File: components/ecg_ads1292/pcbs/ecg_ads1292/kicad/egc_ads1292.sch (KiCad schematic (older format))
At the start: 32 parts, among them J1 n.p., J2 n.p., J3 n.p., J4 n.p., J5 Conn_02x06_Odd_Even

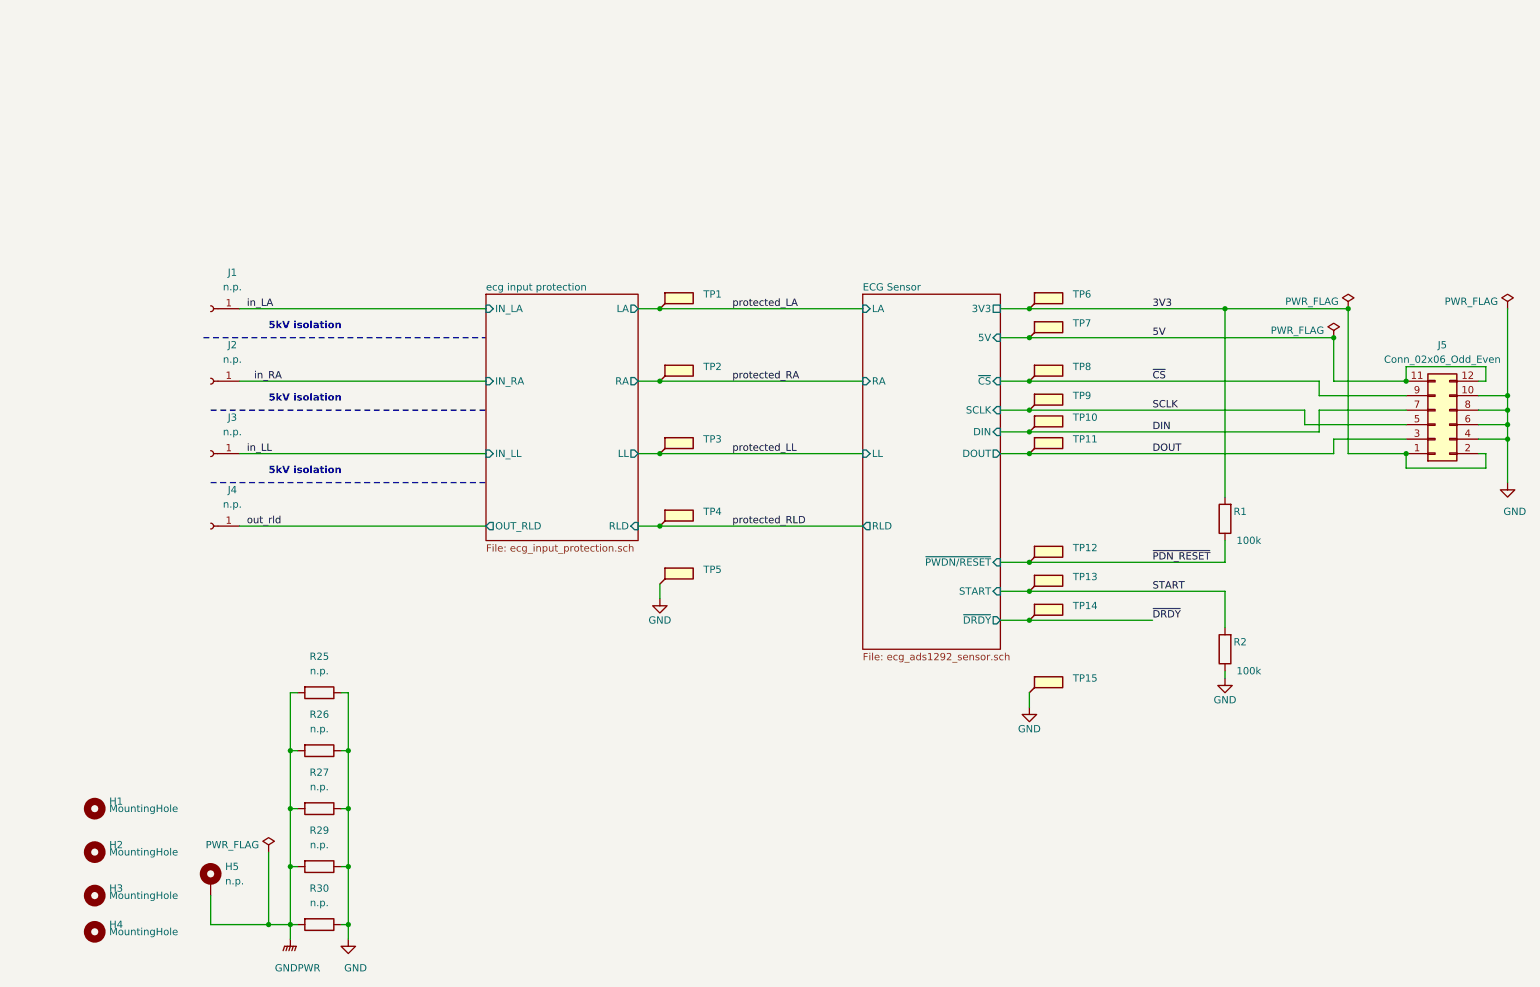
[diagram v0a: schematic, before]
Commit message: allow daisy chaining and improve ground planes
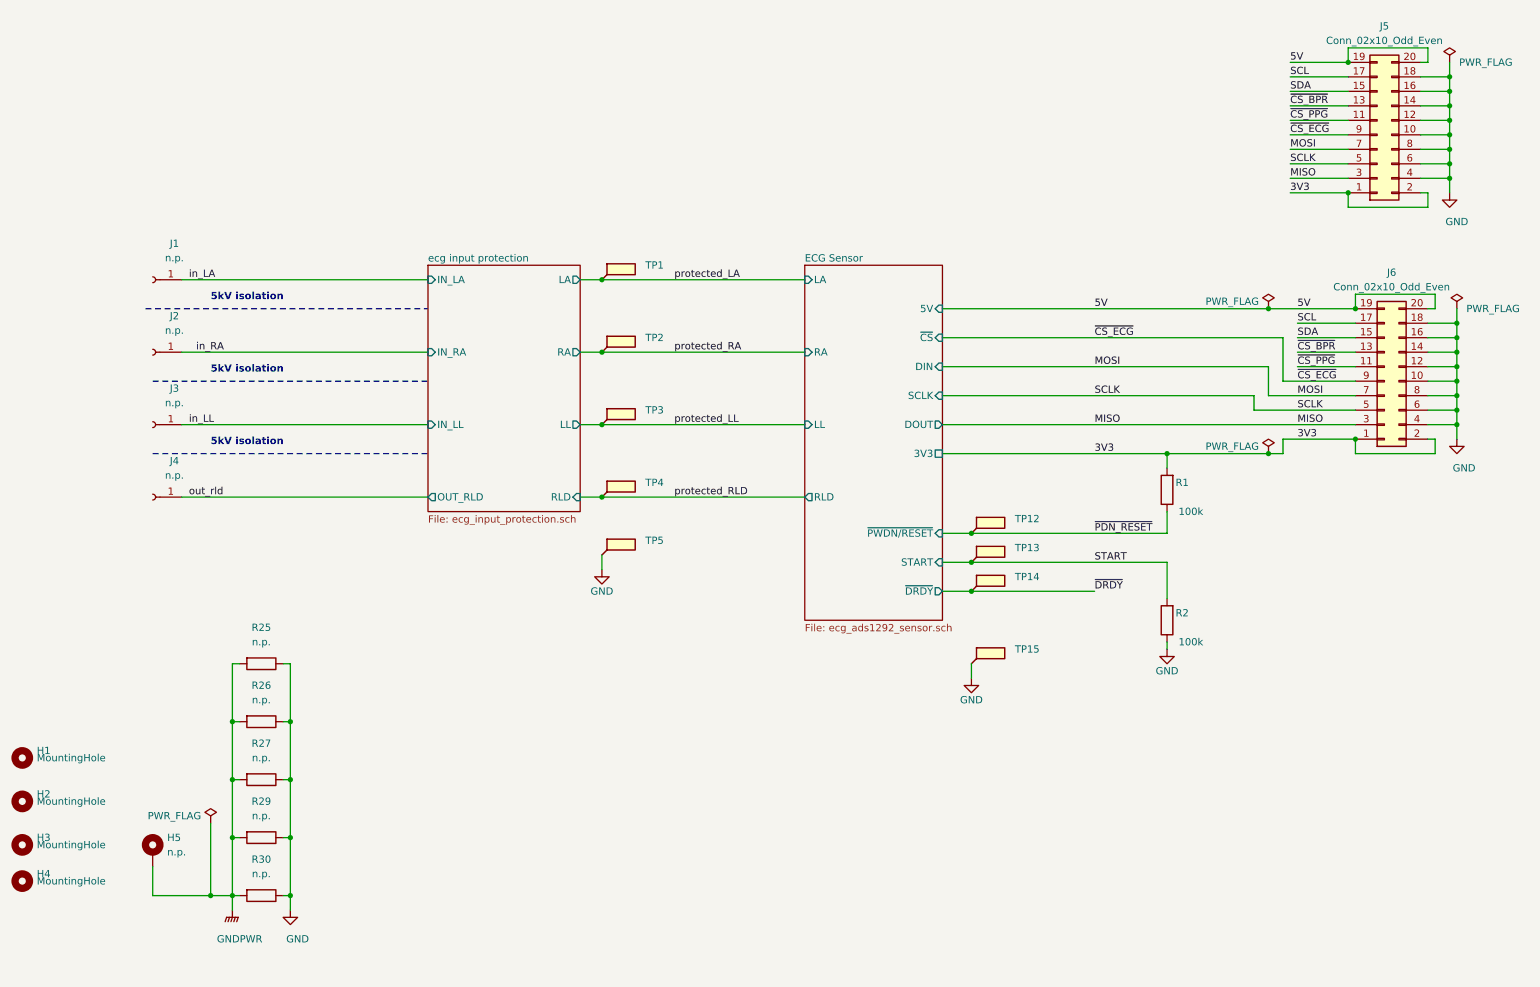
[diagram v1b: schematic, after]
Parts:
- removed J5: Conn_02x06_Odd_Even, Connector_PinHeader_2.54mm:PinHeader_2x06_P2.54mm_Vertical, symbol Connector_Generic:Conn_02x06_Odd_Even
- removed TP10, TP11, TP6, TP7, TP8, TP9: (no value), TestPoint:TestPoint_Loop_D2.50mm_Drill1.0mm, symbol Connector:TestPoint_Flag
- added J5, J6: Conn_02x10_Odd_Even, Connector_IDC:IDC-Header_2x10_P2.54mm_Vertical_Lock, symbol Connector_Generic:Conn_02x10_Odd_Even
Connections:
- net 3V3: now also J5.1 (Pin_1), J5.2 (Pin_2), J6.1 (Pin_1), J6.2 (Pin_2)
- net 5V: now also J5.19 (Pin_19), J5.20 (Pin_20), J6.19 (Pin_19), J6.20 (Pin_20)
- net GND: now also J5.10 (Pin_10), J5.12 (Pin_12), J5.14 (Pin_14), J5.16 (Pin_16), J5.18 (Pin_18), J5.4 (Pin_4), J5.6 (Pin_6), J5.8 (Pin_8), J6.10 (Pin_10), J6.12 (Pin_12), J6.14 (Pin_14), J6.16 (Pin_16), J6.18 (Pin_18), J6.4 (Pin_4), J6.6 (Pin_6), J6.8 (Pin_8)
- net SCLK: now also J5.5 (Pin_5), J6.5 (Pin_5)
- new net MISO: J5.3 (Pin_3), J6.3 (Pin_3)
- new net MOSI: J5.7 (Pin_7), J6.7 (Pin_7)
- new net SCL: J5.17 (Pin_17), J6.17 (Pin_17)
- new net SDA: J5.15 (Pin_15), J6.15 (Pin_15)
- new net ~CS_BPR: J5.13 (Pin_13), J6.13 (Pin_13)
- new net ~CS_ECG: J5.9 (Pin_9), J6.9 (Pin_9)
- new net ~CS_PPG: J5.11 (Pin_11), J6.11 (Pin_11)
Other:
- moved on the sheet: H1, H2, H3, H4, H5, J1, J2, J3, J4, R1, R2, R25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

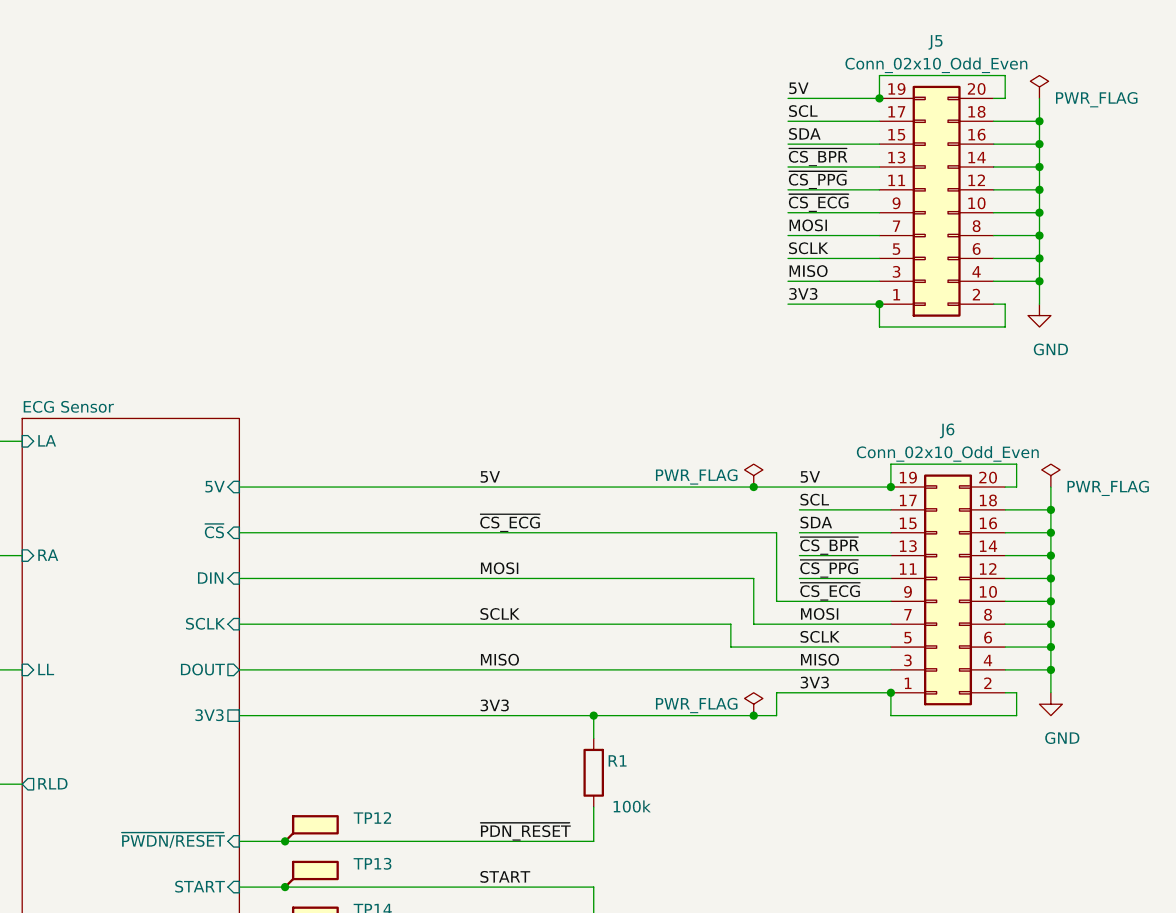
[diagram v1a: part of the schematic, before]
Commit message: orientation of pin headers in schematic matches pcb
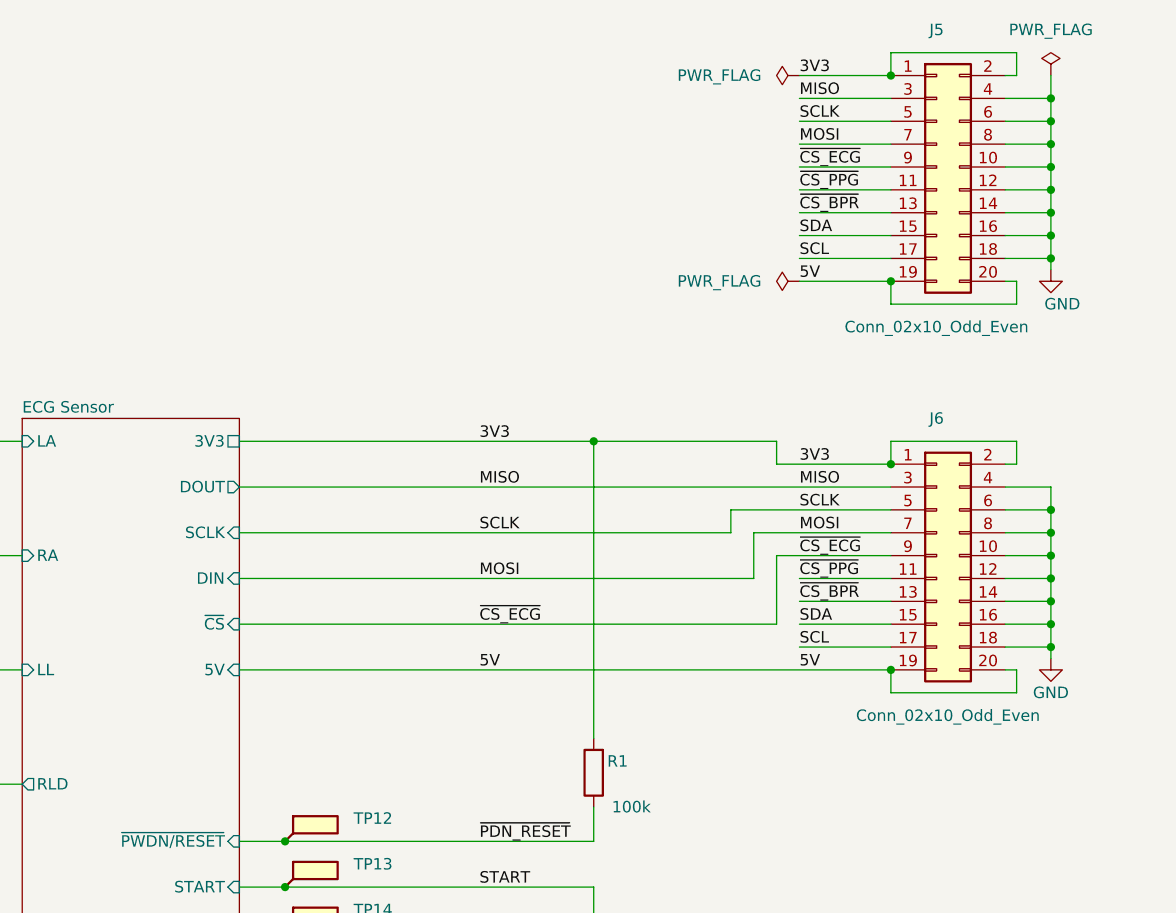
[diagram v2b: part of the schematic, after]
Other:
- moved on the sheet: J5, J6

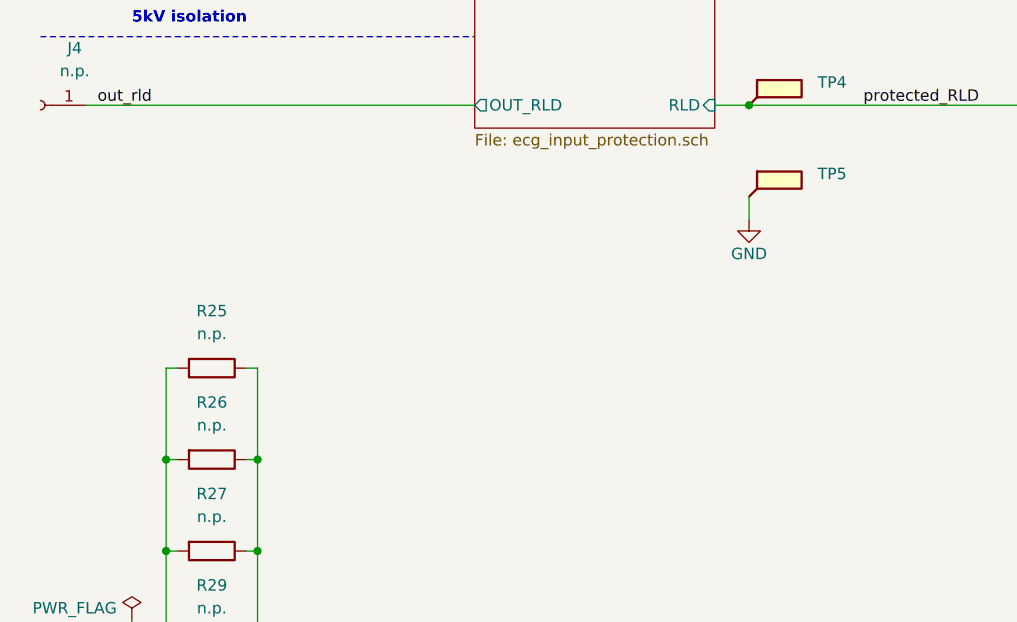
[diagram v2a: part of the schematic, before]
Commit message: add gnd/gndpwr bridge at analog power supply
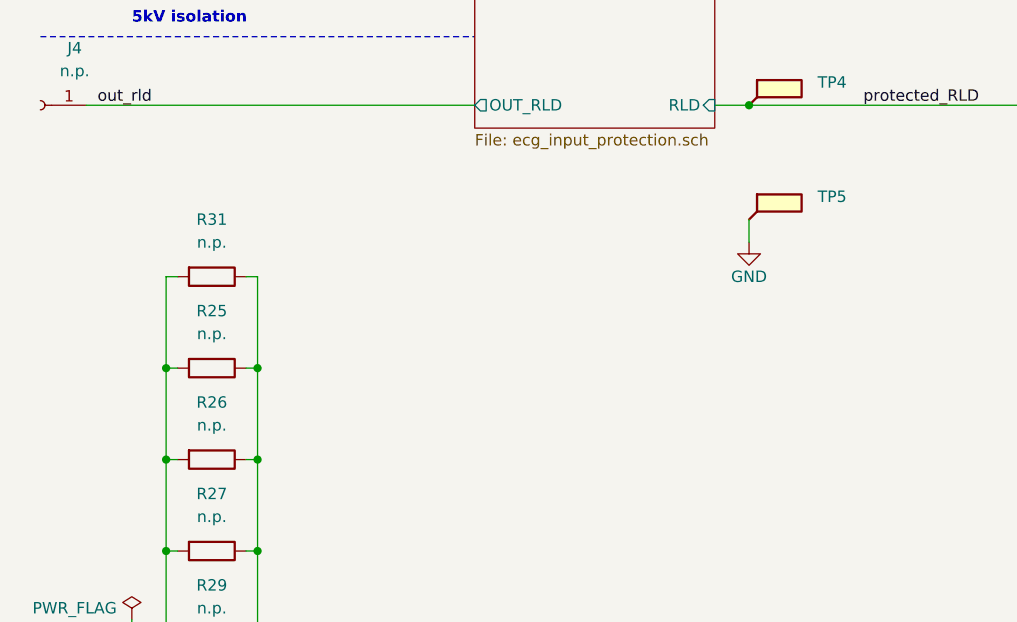
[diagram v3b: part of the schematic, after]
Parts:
- added R31: n.p., Resistor_SMD:R_0815_2038Metric_Pad1.53x4.00mm_HandSolder, symbol component:R
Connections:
- net GND: now also R31.1
- net GNDPWR: now also R31.2
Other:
- moved on the sheet: TP5
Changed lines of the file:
@@
-$EndComp
-$Comp
-L component:GND #PWR?
-U 1 1 5EB18F02
-P 4800 4800
-AR Path="/5E8EE786/5EB18F02" Ref="#PWR?"  Part="1"
-AR Path="/5EB18F02" Ref="#PWR01"  Part="1"
-F 0 "#PWR01" H 4800 4550 50  0001 C CNN
-F 1 "GND" H 4800 4650 50  0000 C CNN
-F 2 "" H 4800 4800 50  0001 C CNN
-F 3 "" H 4800 4800 50  0001 C CNN
-	1    4800 4800
-	1    0    0    -1
-$EndComp
-$Comp
-L Connector:TestPoint_Flag TP5
-U 1 1 5EB28150
-P 4800 4700
-F 0 "TP5" H 5100 4800 50  0000 L CNN
-F 1 " " H 5100 4700 50  0000 L CNN
-F 2 "TestPoint:TestPoint_Loop_D2.50mm_Drill1.0mm" H 5000 4700 50  0001 C CNN
-F 3 "~" H 5000 4700 50  0001 C CNN
-	1    4800 4700
-	1    0    0    -1
 $EndComp
 $Comp
@@
 Wire Wire Line
 	7350 5450 7350 5550
-Wire Wire Line
-	4800 4700 4800 4800
 Text Label 5300 2800 0    50   ~ 0
 protected_LA
@@
 Connection ~ 2250 5850
 Wire Wire Line
-	2250 5850 2250 5450
-Wire Wire Line
 	2600 5850 2650 5850
 Connection ~ 2650 5850
@@
 Wire Wire Line
 	8700 2800 9500 2800
+$Comp
+L component:R R31
+U 1 1 5E9D9425
+P 2450 5050
+F 0 "R31" V 2200 5050 50  0000 C CNN
+F 1 "n.p." V 2300 5050 50  0000 C CNN
+F 2 "Resistor_SMD:R_0815_2038Metric_Pad1.53x4.00mm_HandSolder" V 2380 5050 50  0001 C CNN
+F 3 "" H 2450 5050 50  0001 C CNN
+	1    2450 5050
+	0    1    1    0
+$EndComp
+Wire Wire Line
+	2250 5050 2300 5050
+Wire Wire Line
+	2250 5050 2250 5450
+Connection ~ 2250 5450
+Wire Wire Line
+	2250 5450 2250 5850
+Wire Wire Line
+	4800 4800 4800 4900
+$Comp
+L Connector:TestPoint_Flag TP5
+U 1 1 5EB28150
+P 4800 4800
+F 0 "TP5" H 5100 4900 50  0000 L CNN
+F 1 " " H 5100 4800 50  0000 L CNN
+F 2 "TestPoint:TestPoint_Loop_D2.50mm_Drill1.0mm" H 5000 4800 50  0001 C CNN
+F 3 "~" H 5000 4800 50  0001 C CNN
+	1    4800 4800
+	1    0    0    -1
+$EndComp
+$Comp
+L component:GND #PWR?
+U 1 1 5EB18F02
+P 4800 4900
+AR Path="/5E8EE786/5EB18F02" Ref="#PWR?"  Part="1"
+AR Path="/5EB18F02" Ref="#PWR01"  Part="1"
+F 0 "#PWR01" H 4800 4650 50  0001 C CNN
+F 1 "GND" H 4800 4750 50  0000 C CNN
+F 2 "" H 4800 4900 50  0001 C CNN
+F 3 "" H 4800 4900 50  0001 C CNN
+	1    4800 4900
+	1    0    0    -1
+$EndComp
+Wire Wire Line
+	2650 5450 2650 5050
+Wire Wire Line
+	2650 5050 2600 5050
+Connection ~ 2650 5450
 $EndSCHEMATC
